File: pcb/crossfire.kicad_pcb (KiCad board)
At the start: 4 copper layers, 100 x 80 mm, 0 parts

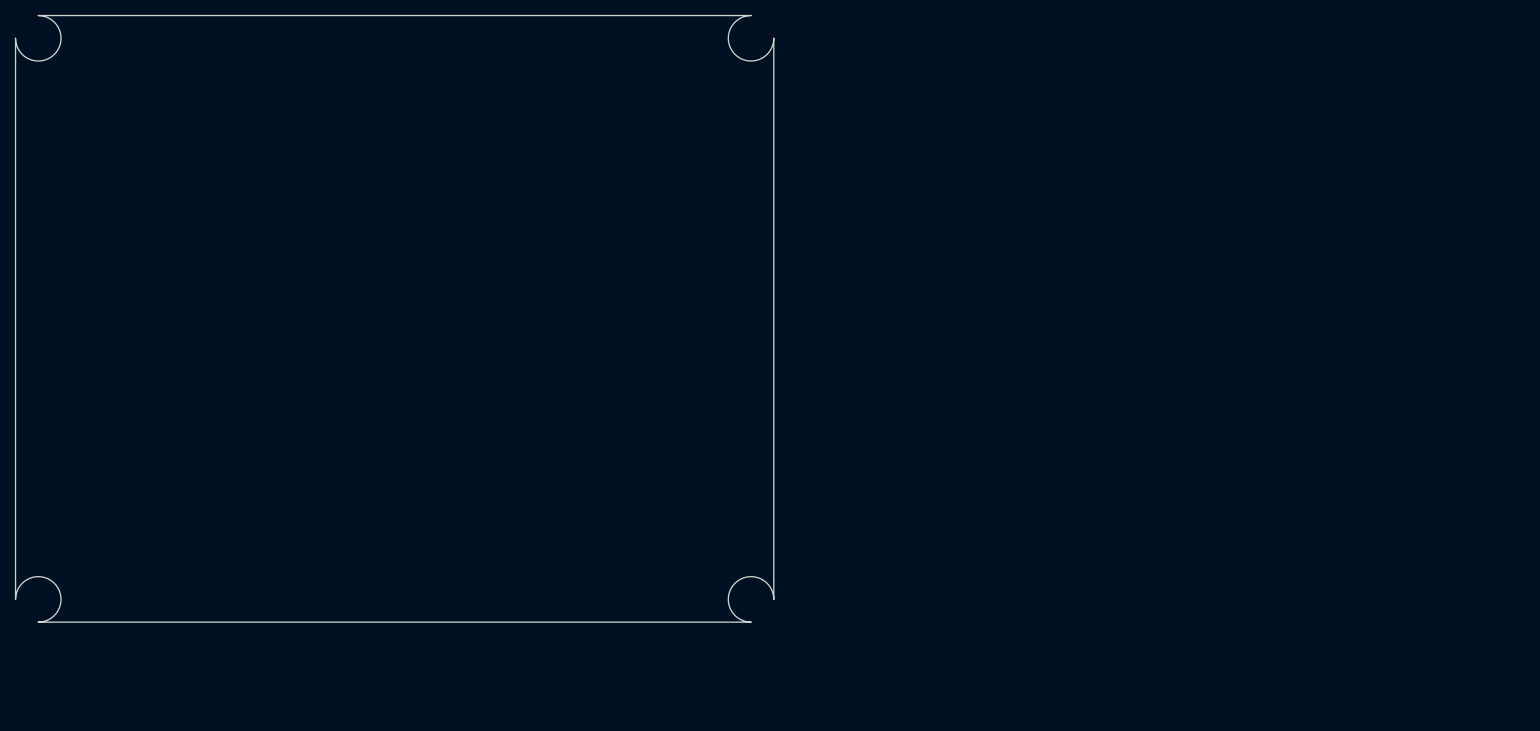
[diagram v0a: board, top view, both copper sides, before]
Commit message: restore the net classes, which the editor had overwritten
Importing the schematic populated the board correctly -- 144 footprints, which is the netlist's 147
components less the three power flags that are virtual and rightly have none, with nothing missing
and nothing extra, and 154 nets all correctly named.

What did not survive was the net classes. They had been written into the project file while the
editor held that file in memory, so the editor's save replaced them. They are back now, applied
with the project closed, and this time checked by resolving them against the board rather than by
reading the file back: 24 nets on the pair class, 8 on Power, 5 on Power+, 3 on Battery and the
remaining 114 -- ground and the local signals -- on Default.

The Signal class is dropped. It was defined at the same 0.20mm as Default and then given no
patterns, so it was an empty class that reads like an oversight. Default is the signal class.

The lesson is worth stating because it has now bitten twice in opposite directions. The footprint
library table was created after the editor had opened the project, so the editor never read it. The
net classes were changed while the editor held the project, so the editor overwrote them. Project
files have two authors whenever KiCad is open, and the schematic and board files are no different.

Co-Authored-By: Claude Opus 5 (1M context) <noreply@anthropic.com>
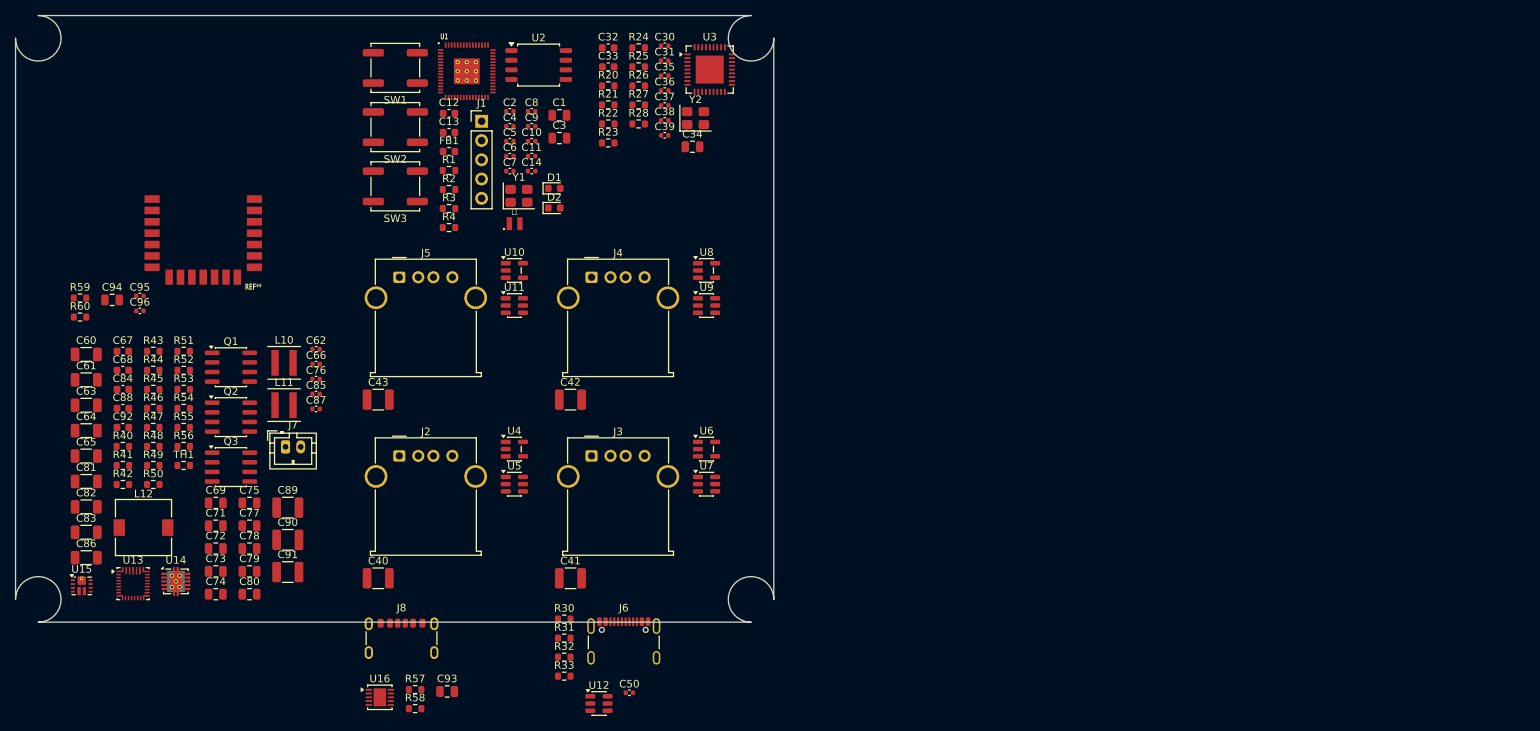
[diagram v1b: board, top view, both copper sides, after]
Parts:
- added C1: 4u7, Capacitor_SMD:C_0805_2012Metric, F.Cu at (71.7, 13.2)
- added C10: 100n, Capacitor_SMD:C_0402_1005Metric, F.Cu at (68.1, 16.6)
- added C11: 100n, Capacitor_SMD:C_0402_1005Metric, F.Cu at (68.1, 18.5)
- added C12: 15p, Capacitor_SMD:C_0603_1608Metric, F.Cu at (57.2, 12.9)
- added C13: 15p, Capacitor_SMD:C_0603_1608Metric, F.Cu at (57.2, 15.4)
- added C14: 100n, Capacitor_SMD:C_0402_1005Metric, F.Cu at (68.1, 20.5)
- added C2: 100n, Capacitor_SMD:C_0402_1005Metric, F.Cu at (65.2, 12.6)
- added C3: 10u, Capacitor_SMD:C_0805_2012Metric, F.Cu at (71.7, 16.2)
- added C30: 100n, Capacitor_SMD:C_0402_1005Metric, F.Cu at (85.6, 3.98)
- added C31: 100n, Capacitor_SMD:C_0402_1005Metric, F.Cu at (85.6, 5.96)
- added C32: 18p, Capacitor_SMD:C_0603_1608Metric, F.Cu at (78.2, 4.25)
- added C33: 18p, Capacitor_SMD:C_0603_1608Metric, F.Cu at (78.2, 6.76)
- added C34: 10u, Capacitor_SMD:C_0805_2012Metric, F.Cu at (89.3, 17.3)
- added C35: 100n, Capacitor_SMD:C_0402_1005Metric, F.Cu at (85.6, 7.92)
- added C36: 100n, Capacitor_SMD:C_0402_1005Metric, F.Cu at (85.6, 9.89)
- added C37: 100n, Capacitor_SMD:C_0402_1005Metric, F.Cu at (85.6, 11.9)
- added C38: 100n, Capacitor_SMD:C_0402_1005Metric, F.Cu at (85.6, 13.8)
- added C39: 100n, Capacitor_SMD:C_0402_1005Metric, F.Cu at (85.6, 15.8)
- added C4: 100n, Capacitor_SMD:C_0402_1005Metric, F.Cu at (65.2, 14.6)
- added C40: 22u, Capacitor_SMD:C_1210_3225Metric, F.Cu at (47.8, 74.2)
- added C41: 22u, Capacitor_SMD:C_1210_3225Metric, F.Cu at (73.2, 74.2)
- added C42: 22u, Capacitor_SMD:C_1210_3225Metric, F.Cu at (73.2, 50.7)
- added C43: 22u, Capacitor_SMD:C_1210_3225Metric, F.Cu at (47.8, 50.7)
- added C5: 100n, Capacitor_SMD:C_0402_1005Metric, F.Cu at (65.2, 16.6)
- added C50: 100n, Capacitor_SMD:C_0402_1005Metric, F.Cu at (81.0, 89.3)
- added C6: 100n, Capacitor_SMD:C_0402_1005Metric, F.Cu at (65.2, 18.5)
- added C60: 10u, Capacitor_SMD:C_1206_3216Metric, F.Cu at (9.32, 44.7)
- added C61: 10u, Capacitor_SMD:C_1206_3216Metric, F.Cu at (9.32, 48.0)
- added C62: 100n, Capacitor_SMD:C_0402_1005Metric, F.Cu at (39.6, 44.0)
- added C63: 10u, Capacitor_SMD:C_1206_3216Metric, F.Cu at (9.32, 51.4)
- added C64: 10u, Capacitor_SMD:C_1206_3216Metric, F.Cu at (9.32, 54.7)
- added C65: 10u, Capacitor_SMD:C_1206_3216Metric, F.Cu at (9.32, 58.1)
- added C66: 100n, Capacitor_SMD:C_0402_1005Metric, F.Cu at (39.6, 46.0)
- added C67: 47n, Capacitor_SMD:C_0603_1608Metric, F.Cu at (14.2, 44.3)
- added C68: 47n, Capacitor_SMD:C_0603_1608Metric, F.Cu at (14.2, 46.8)
- added C69: 4u7, Capacitor_SMD:C_0805_2012Metric, F.Cu at (26.4, 64.3)
- added C7: 100n, Capacitor_SMD:C_0402_1005Metric, F.Cu at (65.2, 20.5)
- added C71: 10u, Capacitor_SMD:C_0805_2012Metric, F.Cu at (26.4, 67.3)
- added C72: 10u, Capacitor_SMD:C_0805_2012Metric, F.Cu at (26.4, 70.3)
- added C73: 10u, Capacitor_SMD:C_0805_2012Metric, F.Cu at (26.4, 73.3)
- added C74: 10u, Capacitor_SMD:C_0805_2012Metric, F.Cu at (26.4, 76.3)
- added C75: 10u, Capacitor_SMD:C_0805_2012Metric, F.Cu at (30.9, 64.3)
- added C76: 100n, Capacitor_SMD:C_0402_1005Metric, F.Cu at (39.6, 47.9)
- added C77: 10u, Capacitor_SMD:C_0805_2012Metric, F.Cu at (30.9, 67.3)
- added C78: 10u, Capacitor_SMD:C_0805_2012Metric, F.Cu at (30.9, 70.3)
- added C79: 10u, Capacitor_SMD:C_0805_2012Metric, F.Cu at (30.9, 73.3)
- added C8: 100n, Capacitor_SMD:C_0402_1005Metric, F.Cu at (68.1, 12.6)
- added C80: 10u, Capacitor_SMD:C_0805_2012Metric, F.Cu at (30.9, 76.3)
- added C81: 22u, Capacitor_SMD:C_1206_3216Metric, F.Cu at (9.32, 61.4)
- added C82: 22u, Capacitor_SMD:C_1206_3216Metric, F.Cu at (9.32, 64.8)
- added C83: 22u, Capacitor_SMD:C_1206_3216Metric, F.Cu at (9.32, 68.1)
- added C84: 10p, Capacitor_SMD:C_0603_1608Metric, F.Cu at (14.2, 49.3)
- added C85: 100n, Capacitor_SMD:C_0402_1005Metric, F.Cu at (39.6, 49.9)
- added C86: 22u, Capacitor_SMD:C_1206_3216Metric, F.Cu at (9.32, 71.5)
- added C87: 100n, Capacitor_SMD:C_0402_1005Metric, F.Cu at (39.6, 51.9)
- added C88: 2u2, Capacitor_SMD:C_0603_1608Metric, F.Cu at (14.2, 51.8)
- added C89: 22u, Capacitor_SMD:C_1210_3225Metric, F.Cu at (35.9, 64.9)
- added C9: 100n, Capacitor_SMD:C_0402_1005Metric, F.Cu at (68.1, 14.6)
- added C90: 22u, Capacitor_SMD:C_1210_3225Metric, F.Cu at (35.9, 69.1)
- added C91: 22u, Capacitor_SMD:C_1210_3225Metric, F.Cu at (35.9, 73.4)
- added C92: 4n7, Capacitor_SMD:C_0603_1608Metric, F.Cu at (14.2, 54.3)
- added C93: 1u, Capacitor_SMD:C_0805_2012Metric, F.Cu at (56.9, 89.1)
- added C94: 10u, Capacitor_SMD:C_0805_2012Metric, F.Cu at (12.7, 37.5)
- added C95: 100n, Capacitor_SMD:C_0402_1005Metric, F.Cu at (16.4, 37.0)
- added C96: 100n, Capacitor_SMD:C_0402_1005Metric, F.Cu at (16.4, 39.0)
- added D1: red, LED_SMD:LED_0603_1608Metric, F.Cu at (71.1, 22.8)
- added D2: green, LED_SMD:LED_0603_1608Metric, F.Cu at (71.1, 25.4)
- added FB1: 600R, Inductor_SMD:L_0603_1608Metric, F.Cu at (57.2, 17.9)
- added J1: SWD+UART, Connector_PinHeader_2.54mm:PinHeader_1x05_P2.54mm_Vertical, F.Cu at (61.5, 13.9)
- added J2: USB_A, Connector_USB:USB_A_Molex_67643_Horizontal, F.Cu at (50.6, 58.1)
- added J3: USB_A, Connector_USB:USB_A_Molex_67643_Horizontal, F.Cu at (76.0, 58.1)
- added J4: USB_A, Connector_USB:USB_A_Molex_67643_Horizontal, F.Cu at (76.0, 34.5)
- added J5: USB_A, Connector_USB:USB_A_Molex_67643_Horizontal, F.Cu at (50.6, 34.5)
- added J6: USB-C data, Connector_USB:USB_C_Receptacle_GCT_USB4105-xx-A_16P_TopMnt_Horizontal, F.Cu at (80.2, 83.6)
- added J7: 1S LiPo, Connector_JST:JST_PH_B2B-PH-K_1x02_P2.00mm_Vertical, F.Cu at (35.6, 56.9)
- added J8: USB-C power, Connector_USB:USB_C_Receptacle_GCT_USB4125-xx-x_6P_TopMnt_Horizontal, F.Cu at (50.9, 83.2)
- added L1: 3u3, crossfire:abracon_aota-b201610s3r3-101-t, F.Cu at (65.8, 27.5)
- added L10: 1u0, Inductor_SMD:L_Coilcraft_XxL4030, F.Cu at (35.4, 45.8)
- added L11: 1u0, Inductor_SMD:L_Coilcraft_XxL4030, F.Cu at (35.4, 51.4)
- added L12: 2u2, Inductor_SMD:L_7.3x7.3_H4.5, F.Cu at (16.9, 67.5)
- added Q1: Q_Dual_NMOS_S1G1S2G2D2D2D1D1, Package_SO:SOIC-8_3.9x4.9mm_P1.27mm, F.Cu at (28.4, 46.4)
- added Q2: Q_Dual_NMOS_S1G1S2G2D2D2D1D1, Package_SO:SOIC-8_3.9x4.9mm_P1.27mm, F.Cu at (28.4, 53.0)
- added Q3: Q_Dual_NMOS_S1G1S2G2D2D2D1D1, Package_SO:SOIC-8_3.9x4.9mm_P1.27mm, F.Cu at (28.4, 59.5)
- added R1: 1k, Resistor_SMD:R_0603_1608Metric, F.Cu at (57.2, 20.4)
- added R2: 10k, Resistor_SMD:R_0603_1608Metric, F.Cu at (57.2, 22.9)
- added R20: 12k, Resistor_SMD:R_0603_1608Metric, F.Cu at (78.2, 9.28)
- added R21: 10k, Resistor_SMD:R_0603_1608Metric, F.Cu at (78.2, 11.8)
- added R22: 10k, Resistor_SMD:R_0603_1608Metric, F.Cu at (78.2, 14.3)
- added R23: 27R, Resistor_SMD:R_0603_1608Metric, F.Cu at (78.2, 16.8)
- added R24: 27R, Resistor_SMD:R_0603_1608Metric, F.Cu at (82.2, 4.25)
- added R25: 10k, Resistor_SMD:R_0603_1608Metric, F.Cu at (82.2, 6.76)
- added R26: 100k, Resistor_SMD:R_0603_1608Metric, F.Cu at (82.2, 9.28)
- added R27: 15k, Resistor_SMD:R_0603_1608Metric, F.Cu at (82.2, 11.8)
- added R28: 15k, Resistor_SMD:R_0603_1608Metric, F.Cu at (82.2, 14.3)
- added R3: 1k, Resistor_SMD:R_0603_1608Metric, F.Cu at (57.2, 25.5)
- added R30: 5k1, Resistor_SMD:R_0603_1608Metric, F.Cu at (72.4, 79.6)
- added R31: 5k1, Resistor_SMD:R_0603_1608Metric, F.Cu at (72.4, 82.1)
- added R32: 100k, Resistor_SMD:R_0603_1608Metric, F.Cu at (72.4, 84.6)
- added R33: 100k, Resistor_SMD:R_0603_1608Metric, F.Cu at (72.4, 87.1)
- added R4: 1k, Resistor_SMD:R_0603_1608Metric, F.Cu at (57.2, 28.0)
- added R40: 10k, Resistor_SMD:R_0603_1608Metric, F.Cu at (14.2, 56.8)
- added R41: 10k, Resistor_SMD:R_0603_1608Metric, F.Cu at (14.2, 59.3)
- added R42: 10k, Resistor_SMD:R_0603_1608Metric, F.Cu at (14.2, 61.8)
- added R43: 10k, Resistor_SMD:R_0603_1608Metric, F.Cu at (18.2, 44.3)
- added R44: 3k0, Resistor_SMD:R_0603_1608Metric, F.Cu at (18.2, 46.8)
- added R45: 5k23, Resistor_SMD:R_0603_1608Metric, F.Cu at (18.2, 49.3)
- added R46: 30k1, Resistor_SMD:R_0603_1608Metric, F.Cu at (18.2, 51.8)
- added R47: 10k, Resistor_SMD:R_0603_1608Metric, F.Cu at (18.2, 54.3)
- added R48: 100R, Resistor_SMD:R_0603_1608Metric, F.Cu at (18.2, 56.8)
- added R49: 1M, Resistor_SMD:R_0603_1608Metric, F.Cu at (18.2, 59.3)
- added R50: 178k, Resistor_SMD:R_0603_1608Metric, F.Cu at (18.2, 61.8)
- added R51: 316k, Resistor_SMD:R_0603_1608Metric, F.Cu at (22.2, 44.3)
- added R52: 100k, Resistor_SMD:R_0603_1608Metric, F.Cu at (22.2, 46.8)
- added R53: 332k, Resistor_SMD:R_0603_1608Metric, F.Cu at (22.2, 49.3)
- added R54: 107k, Resistor_SMD:R_0603_1608Metric, F.Cu at (22.2, 51.8)
- added R55: 17k4, Resistor_SMD:R_0603_1608Metric, F.Cu at (22.2, 54.3)
- added R56: 174k, Resistor_SMD:R_0603_1608Metric, F.Cu at (22.2, 56.8)
- added R57: 6.04k, Resistor_SMD:R_0603_1608Metric, F.Cu at (52.7, 88.9)
- added R58: 10.5k, Resistor_SMD:R_0603_1608Metric, F.Cu at (52.7, 91.4)
- added R59: 470R, Resistor_SMD:R_0603_1608Metric, F.Cu at (8.51, 37.3)
- added R60: 10k, Resistor_SMD:R_0603_1608Metric, F.Cu at (8.51, 39.8)
- added SW1: BOOT, Button_Switch_SMD:SW_Push_1P1T_NO_CK_KSC6xxJ, F.Cu at (50.1, 6.91)
- added SW2: RESET, Button_Switch_SMD:SW_Push_1P1T_NO_CK_KSC6xxJ, F.Cu at (50.1, 14.7)
- added SW3: USER, Button_Switch_SMD:SW_Push_1P1T_NO_CK_KSC6xxJ, F.Cu at (50.1, 22.5)
- added TH1: 10k B3435, Resistor_SMD:R_0603_1608Metric, F.Cu at (22.2, 59.3)
- added U1: RP2350A, crossfire:rpi_rp2350a_vias, F.Cu at (59.5, 7.35)
- added U10: TPS2065C, Package_TO_SOT_SMD:SOT-23-5, F.Cu at (65.8, 33.6)
- added U11: USBLC6-2SC6, Package_TO_SOT_SMD:SOT-23-6, F.Cu at (65.8, 38.2)
- added U12: USBLC6-2SC6, Package_TO_SOT_SMD:SOT-23-6, F.Cu at (76.9, 90.7)
- added U13: BQ25798, Package_DFN_QFN:Texas_RQM0029A_VQFN-29_4x4mm_P0.4mm, F.Cu at (15.5, 74.9)
- added U14: TPS63060, Package_SON:Texas_DSC0010J_ThermalVias, F.Cu at (21.1, 74.6)
- added U15: TPS61089, Package_DFN_QFN:Texas_VQFN-RNR0011A-11, F.Cu at (8.72, 75.2)
- added U16: HUSB238, Package_DFN_QFN:DFN-10-1EP_3x3mm_P0.5mm_EP1.65x2.38mm, F.Cu at (48.0, 89.9)
- added U17: RM2, crossfire:rpi_rmc20452t, F.Cu at (24.8, 26.8)
- added U2: W25Q128JVS, Package_SO:SOIC-8_5.3x5.3mm_P1.27mm, F.Cu at (69.0, 6.53)
- added U3: USB2514B, Package_DFN_QFN:QFN-36-1EP_6x6mm_P0.5mm_EP3.7x3.7mm, F.Cu at (91.5, 7.12)
- added U4: TPS2065C, Package_TO_SOT_SMD:SOT-23-5, F.Cu at (65.8, 57.2)
- added U5: USBLC6-2SC6, Package_TO_SOT_SMD:SOT-23-6, F.Cu at (65.8, 61.8)
- added U6: TPS2065C, Package_TO_SOT_SMD:SOT-23-5, F.Cu at (91.1, 57.2)
- added U7: USBLC6-2SC6, Package_TO_SOT_SMD:SOT-23-6, F.Cu at (91.1, 61.8)
- added U8: TPS2065C, Package_TO_SOT_SMD:SOT-23-5, F.Cu at (91.1, 33.6)
- added U9: USBLC6-2SC6, Package_TO_SOT_SMD:SOT-23-6, F.Cu at (91.1, 38.2)
- added Y1: 12MHz, Crystal:Crystal_SMD_3225-4Pin_3.2x2.5mm, F.Cu at (66.4, 23.8)
- added Y2: 24MHz, Crystal:Crystal_SMD_3225-4Pin_3.2x2.5mm, F.Cu at (89.7, 13.5)

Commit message: lay out the floorplan, and make the antenna keep-out a rule rather than a drawing
Thirty-one parts placed, the rest parked off the board on purpose: anything still outside the
outline is something not yet thought about, which is a more useful state than a part sitting where
the importer dropped it and looking deliberate.

The order was to place what cannot move first and fit the rest around it. Four receptacles on
25.4mm centres along the bottom edge, mouths flush. The upstream pair on the opposite edge, so a
host cable and the instruments leave by different ends. The radio with its antenna end flush to the
top edge, so the keep-out falls off the board rather than costing 35mm of copper. Power down the
left in the order it flows -- sink, both input switches, charger, converters. Processor between the
connector it serves and the hub it drives, hub low and central so no port is much further from it
than any other. Controls and indicators on the right edge.

Checked numerically rather than by eye, which caught three things a drawing would not have: the
radio's body is centred on its footprint origin rather than offset, so the first attempt hung it
4.7mm off the board; and two pairs of courtyards overlapped.

The thermistor moved twice and the second move is the interesting one. Beside the cell connector it
sat 7.8mm from the boost's inductor, which is the constraint recorded for it being broken on the
first attempt. But its line is a divider tap carrying microamps, so length costs nothing while heat
costs a false reading and a refusal to charge a good cell. It now sits on the coolest open ground
on the board with the nearest converter 44mm away, and the enclosure must put the cell over it.

The radio's keep-out was marked only on the fabrication layer by its vendor -- documented but not
enforced, so a ground pour would have filled the antenna's clearance with nothing objecting. It is
now a rule area on all four copper layers over the part of the region that lands on th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
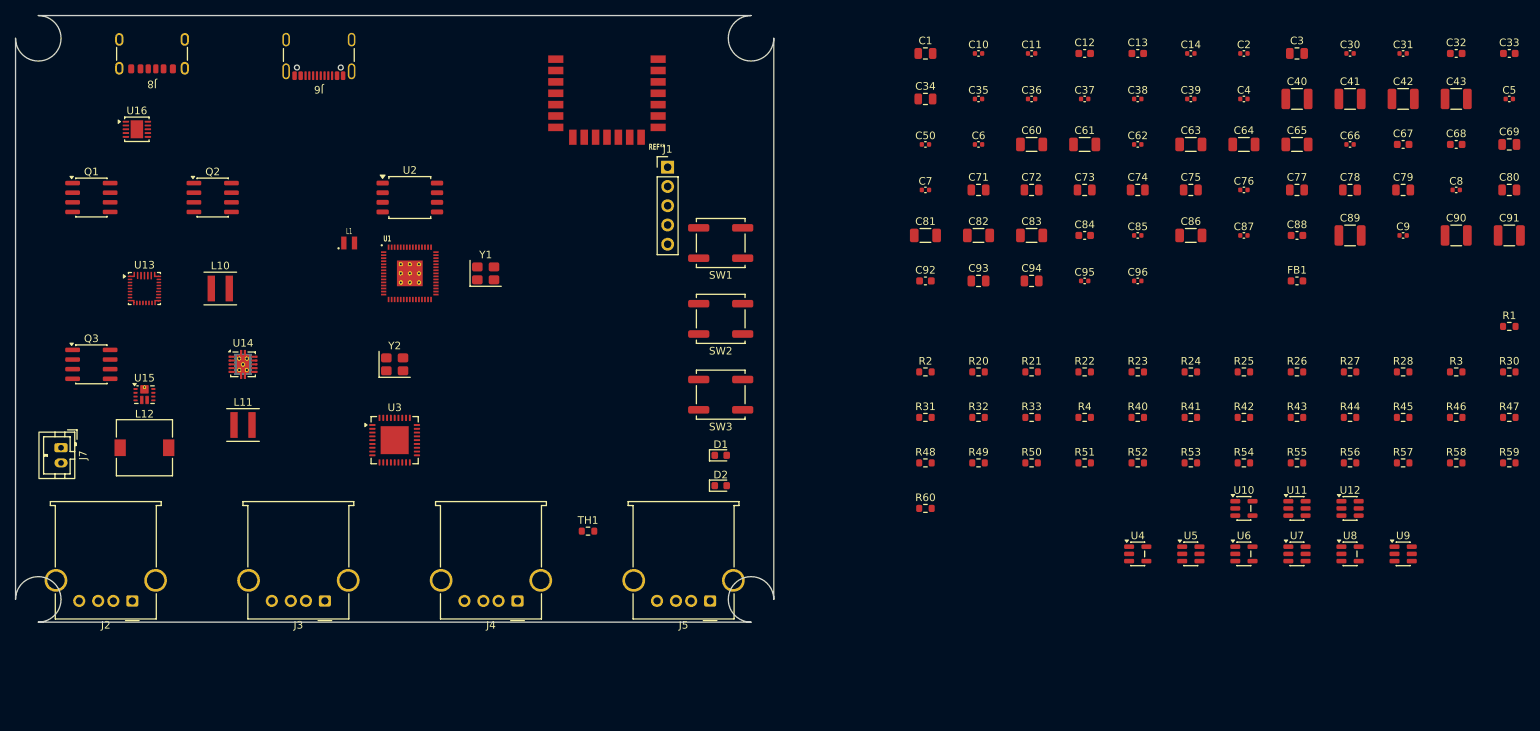
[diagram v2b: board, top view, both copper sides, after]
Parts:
- moved R59 189.7 mm to (197.0, 59.0)
- moved R47 178.8 mm to (197.0, 53.0)
- moved C68 178.3 mm to (190.0, 17.0)
- moved C69 177.0 mm to (197.0, 17.0)
- moved C80 174.5 mm to (197.0, 23.0)
- moved R46 171.8 mm to (190.0, 53.0)
- moved C67 171.0 mm to (183.0, 17.0)
- moved C91 167.1 mm to (197.0, 29.0)
- moved C65 164.9 mm to (169.0, 17.0)
- moved R45 164.9 mm to (183.0, 53.0)
- moved C79 160.2 mm to (183.0, 23.0)
- moved C90 159.2 mm to (190.0, 29.0)
- moved R44 158.0 mm to (176.0, 53.0)
- moved C64 157.3 mm to (162.0, 17.0)
- moved C88 156.5 mm to (169.0, 29.0)
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
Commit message: clear the board rules check, and correct the claim that it was already clear
The previous commit's message says "board check passes with no violations". That is false. There
were seventy-one, and I read a truncated report rather than its count line. The check is clear now,
and this records what it took, because two of the three causes were rules set tighter than the parts
can be built to:

Clearance was 0.2mm. The processor's pads are on 0.4mm pitch and 0.23mm across, so the gap from one
pad to the next is 0.17mm -- a property of the package, which no board carrying the part can satisfy.
A class clearance is a routing figure and a pad field cannot honour one, so the floor is 0.15mm
uniformly, including on the power classes. Nothing is given away: IPC-2221 asks 0.1mm between
uncoated external conductors below 30V and the highest potential here is a 20V supply contract. The
heavy rails still get more room wherever the layout allows, as practice rather than as a rule the
parts break.

The smallest hole was 0.25mm. The boost converter's thermal pad carries 0.2mm vias, deliberately
small so solder does not wick down them and starve the joint; through 1.6mm of board that is an 8:1
aspect ratio, which is ordinary capability.

Hole clearance was set from the wrong key the first time -- hole-to-hole lowered, hole-to-copper left
at 0.25mm, which is why the data connector kept failing after it should have stopped.

The two remaining were geometry: 3mm corners cut far enough across to reach the outer receptacles'
shield pads, so the radius is set by the parts nearest the corners rather than by taste, and the
debug header sat under the radio's outline.

The last one is a defect in an imported footprint rather than in this layout. The radio module's
footprint has its reference field hidden and a plain text reading REF** visible in its place, so the
part would have been silkscreened with the placeholder and never with its designator, on every board
built from it. Fixed in the libr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
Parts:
- moved J1 5.00 mm to (86.0, 25.0)
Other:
- outline, holes or cut-outs redrawn
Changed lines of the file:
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@@
 		(tags "USB_A Female Connector receptacle")
 		(property "Reference" "J4"
-			(at 3.5 -3.19 180)
+			(at 3.5 6.7 180)
 			(layer "F.SilkS")
 			(effects
@@
 		(tags "USB_A Female Connector receptacle")
 		(property "Reference" "J2"
-			(at 3.5 -3.19 180)
+			(at 3.5 6.7 180)
 			(layer "F.SilkS")
 			(effects
@@
 		(tags "USB_A Female Connector receptacle")
 		(property "Reference" "J5"
-			(at 3.5 -3.19 180)
+			(at 3.5 6.7 180)
 			(layer "F.SilkS")
 			(effects
@@
 	(footprint "Connector_PinHeader_2.54mm:PinHeader_1x05_P2.54mm_Vertical"
 		(layer "F.Cu")
-		(at 86 20)
+		(at 86 25)
 		(descr "Through hole straight pin header, 1x05, 2.54mm pitch, single row")
 		(tags "Through hole pin header THT 1x05 2.54mm single row")
@@
 			(layer "F.Fab")
 		)
-		(fp_text user "REF**"
+		(fp_text user "${REFERENCE}"
 			(at 5.5 9.5 0)
 			(unlocked yes)
@@
 		(tags "USB_A Female Connector receptacle")
 		(property "Reference" "J3"
-			(at 3.5 -3.19 180)
+			(at 3.5 6.7 180)
 			(layer "F.SilkS")
 			(effects
@@
 	)
 	(gr_line
-		(start 0 77)
-		(end 0 3)
+		(start 0 78.5)
+		(end 0 1.5)
 		(stroke
 			(width 0.1)
@@
 	)
 	(gr_arc
-		(start 0 77)
-		(mid 5.12132 74.87868)
-		(end 3 80)
+		(start 0 78.5)
+		(mid 2.56066 77.43934)
+		(end 1.5 80)
 		(stroke
 			(width 0.1)
@@
 	)
 	(gr_arc
-		(start 3 0)
-		(mid 5.12132 5.12132)
-		(end 0 3)
+		(start 1.5 0)
+		(mid 2.56066 2.56066)
+		(end 0 1.5)
 		(stroke
 			(width 0.1)
@@
 	)
 	(gr_line
-		(start 3 0)
-		(end 97 0)
+		(start 1.5 0)
+		(end 98.5 0)
 		(stroke
 			(width 0.1)
@@
 	)
 	(gr_line
-		(start 97 80)
-		(end 3 80)
+		(start 98.5 80)
+		(end 1.5 80)
 		(stroke
 			(width 0.1)
@@
 	)
 	(gr_arc
-		(start 97 80)
-		(mid 94.87868 74.87868)
-		(end 100 77)
+		(start 98.5 80)
+		(mid 97.43934 77.43934)
+		(end 100 78.5)
 		(stroke
 			(width 0.1)
@@
 	)
 	(gr_arc
-		(start 100 3)
-		(mid 94.87868 5.12132)
-		(end 97 0)
+		(start 100 1.5)
+		(mid 97.43934 2.56066)
+		(end 98.5 0)
 		(stroke
 			(width 0.1)
@@
 	)
 	(gr_line
-		(start 100 3)
-		(end 100 77)
+		(start 100 1.5)
+		(end 100 78.5)
 		(stroke
 			(width 0.1)
